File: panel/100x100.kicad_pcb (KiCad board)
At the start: 2 copper layers, 91.1 x 98.6 mm, 65 parts, among them J1 Conn_01x03_Male, J2 USB_B_Micro, SW1 SW_Push, U1 ATtiny9-TS

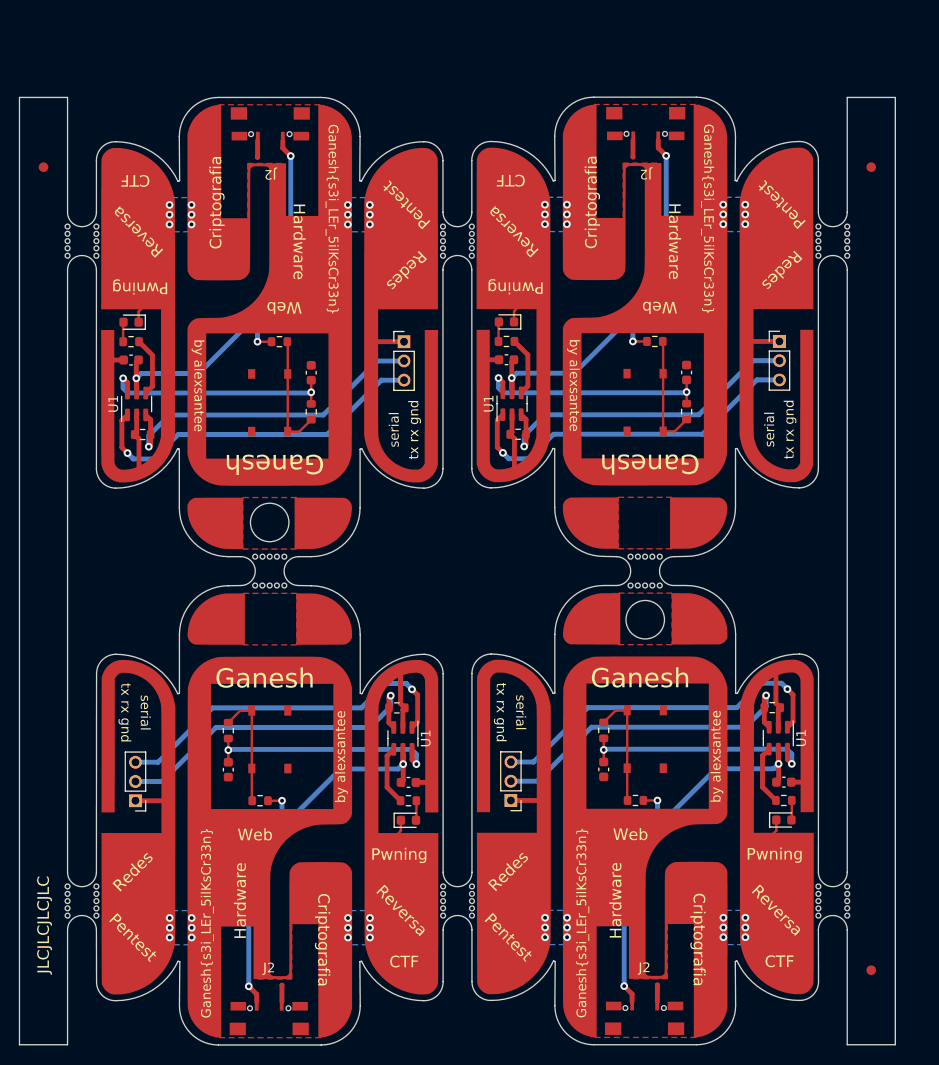
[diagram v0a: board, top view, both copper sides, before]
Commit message: panelization fixes
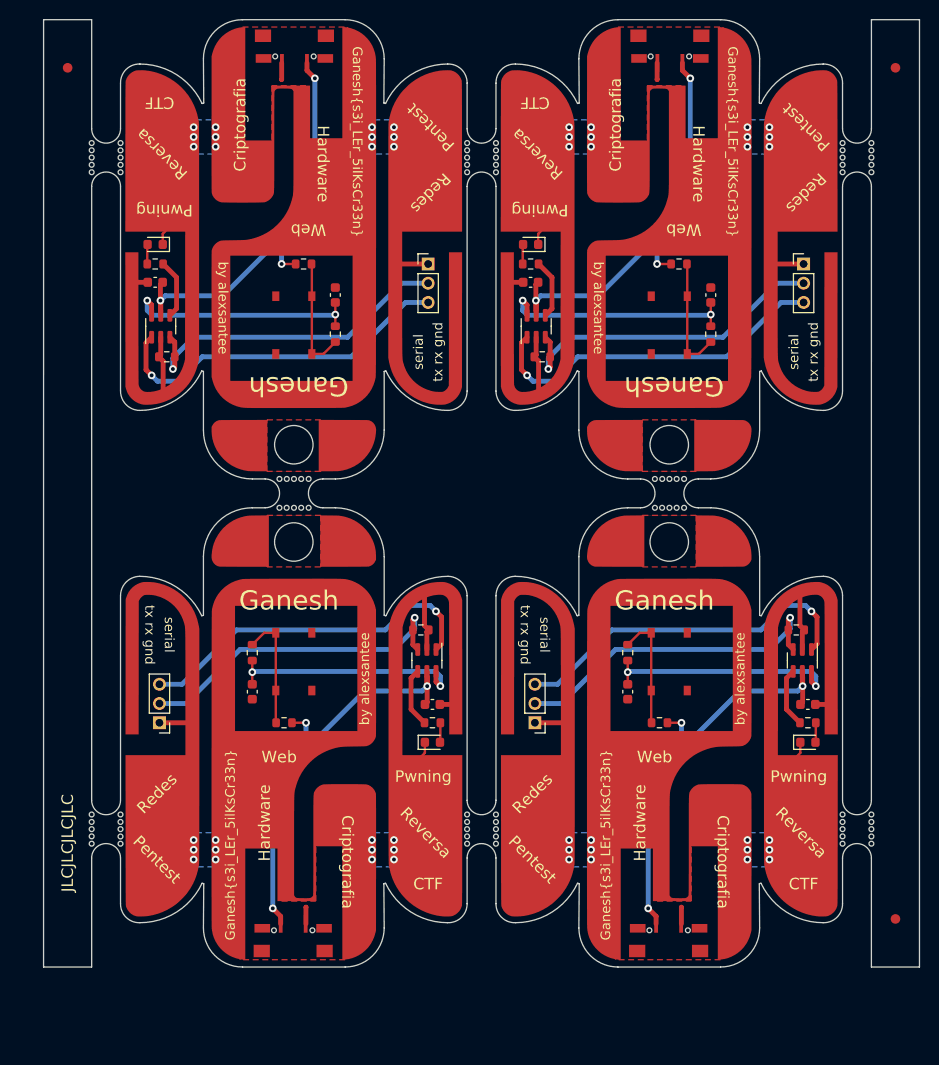
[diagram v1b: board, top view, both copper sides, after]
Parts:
- removed the C1 at (35.4, 56.8)
- removed the C1 at (74.4, 56.7)
- removed the C1 at (64.2, 100.7)
- removed the C1 at (103.3, 100.7)
- removed the C2 at (54.1, 58.1)
- removed the C2 at (93.2, 58.1)
- removed the C2 at (45.5, 99.4)
- removed the C2 at (84.5, 99.3)
- removed the D1 at (64.2, 104.6)
- removed the D1 at (74.4, 52.8)
- removed the D1 at (35.4, 52.8)
- removed the D1 at (103.3, 104.6)
- removed the Hole at (49.8, 73.7)
- removed the Hole at (88.9, 83.8)
- removed the J1 at (74.9, 102.6)
- removed the J1 at (35.9, 102.6)
- removed the J1 at (102.8, 54.8)
- removed the J1 at (63.8, 54.9)
- removed the J2 at (49.8, 127.0)
- removed the J2 at (49.9, 30.5)
- removed the J2 at (88.8, 127.0)
- removed the J2 at (88.9, 30.5)
- removed the Logo_silk at (49.8, 53.3)
- removed the Logo_silk at (88.9, 53.3)
- removed the Logo_silk at (49.8, 104.1)
- removed the Logo_silk at (88.9, 104.1)
- removed the R1 at (63.0, 92.9)
- removed the R1 at (102.1, 92.9)
- removed the R1 at (75.6, 64.5)
- removed the R1 at (36.6, 64.5)
- removed the R2 at (50.8, 54.9)
- removed the R2 at (89.9, 54.8)
- removed the R2 at (48.8, 102.6)
- removed the R2 at (87.9, 102.6)
- removed the R3 at (103.3, 102.6)
- removed the R3 at (74.4, 54.8)
- removed the R3 at (35.4, 54.9)
- removed the R3 at (64.2, 102.6)
- removed the R4 at (54.1, 62.2)
- removed the R4 at (45.5, 95.3)
- removed the R4 at (84.5, 95.3)
- removed the R4 at (93.2, 62.1)
- removed the REF** at (26.3, 36.7)
- removed the REF** at (112.4, 36.7)
- removed the REF** at (112.4, 120.2)
- removed the SW1 at (88.9, 61.2)
- removed the SW1 at (49.8, 96.2)
- removed the SW1 at (49.8, 61.2)
- removed the SW1 at (88.9, 96.2)
- removed the U1 at (36.0, 61.3)
- removed the U1 at (63.7, 96.1)
- removed the U1 at (102.7, 96.1)
- removed the U1 at (75.0, 61.3)
- removed the logo_cobre at (88.9, 53.3)
- removed the logo_cobre at (49.8, 53.3)
- removed the logo_cobre at (49.8, 104.1)
- removed the logo_cobre at (88.9, 104.1)
- removed the mouse-bite-3mm-slot at (49.8, 78.7)
- removed the mouse-bite-3mm-slot at (88.9, 78.7)
- removed the mouse-bite-3mm-slot at (69.3, 113.0)
- removed the mouse-bite-3mm-slot at (69.3, 44.4)
- removed the mouse-bite-3mm-slot at (30.3, 44.4)
- removed the mouse-bite-3mm-slot at (30.3, 113.0)
- removed the mouse-bite-3mm-slot at (108.4, 113.0)
- removed the mouse-bite-3mm-slot at (108.4, 44.4)
- added C1: 100 nF, Capacitor_SMD:C_0603_1608Metric, F.Cu at (66.7, 92.6)
- added C1: 100 nF, Capacitor_SMD:C_0603_1608Metric, F.Cu at (105.8, 92.6)
- added C1: 100 nF, Capacitor_SMD:C_0603_1608Metric, F.Cu at (76.9, 48.7)
- added C1: 100 nF, Capacitor_SMD:C_0603_1608Metric, F.Cu at (37.9, 48.7)
- added C2: 1.5 n, Capacitor_SMD:C_0603_1608Metric, F.Cu at (95.7, 50.0)
- added C2: 1.5 n, Capacitor_SMD:C_0603_1608Metric, F.Cu at (87.0, 91.3)
- added C2: 1.5 n, Capacitor_SMD:C_0603_1608Metric, F.Cu at (56.6, 50.0)
- added C2: 1.5 n, Capacitor_SMD:C_0603_1608Metric, F.Cu at (48.0, 91.3)
- added D1: LED, LED_SMD:LED_0603_1608Metric, F.Cu at (66.7, 96.5)
- added D1: LED, LED_SMD:LED_0603_1608Metric, F.Cu at (37.9, 44.8)
- added D1: LED, LED_SMD:LED_0603_1608Metric, F.Cu at (105.8, 96.5)
- added D1: LED, LED_SMD:LED_0603_1608Metric, F.Cu at (76.9, 44.8)
- added Hole: MountingHole_4mm, MountingHole:MountingHole_4mm, F.Cu at (52.3, 75.7)
- added Hole: MountingHole_4mm, MountingHole:MountingHole_4mm, F.Cu at (52.3, 65.6)
- added Hole: MountingHole_4mm, MountingHole:MountingHole_4mm, F.Cu at (91.4, 65.6)
- added Hole: MountingHole_4mm, MountingHole:MountingHole_4mm, F.Cu at (91.4, 75.7)
- added J1: Conn_01x03_Male, Connector_PinHeader_2.00mm:PinHeader_1x03_P2.00mm_Vertical, F.Cu at (66.3, 46.8)
- added J1: Conn_01x03_Male, Connector_PinHeader_2.00mm:PinHeader_1x03_P2.00mm_Vertical, F.Cu at (105.3, 46.8)
- added J1: Conn_01x03_Male, Connector_PinHeader_2.00mm:PinHeader_1x03_P2.00mm_Vertical, F.Cu at (77.4, 94.5)
- added J1: Conn_01x03_Male, Connector_PinHeader_2.00mm:PinHeader_1x03_P2.00mm_Vertical, F.Cu at (38.4, 94.5)
- added J2: USB_B_Micro, Custom_Footprints:MicroQTJ_2pads, F.Cu at (91.4, 22.4)
- added J2: USB_B_Micro, Custom_Footprints:MicroQTJ_2pads, F.Cu at (52.3, 118.9)
- added J2: USB_B_Micro, Custom_Footprints:MicroQTJ_2pads, F.Cu at (52.4, 22.4)
- added J2: USB_B_Micro, Custom_Footprints:MicroQTJ_2pads, F.Cu at (91.3, 118.9)
- added Logo_silk: LOGO, Logo_Ganesh:35x46_2, B.Cu at (52.3, 96.0)
- added Logo_silk: LOGO, Logo_Ganesh:35x46_2, B.Cu at (91.4, 45.3)
- added Logo_silk: LOGO, Logo_Ganesh:35x46_2, B.Cu at (91.4, 96.0)
- added Logo_silk: LOGO, Logo_Ganesh:35x46_2, B.Cu at (52.3, 45.3)
- added R1: 10 k, Resistor_SMD:R_0603_1608Metric, F.Cu at (104.6, 84.8)
- added R1: 10 k, Resistor_SMD:R_0603_1608Metric, F.Cu at (65.5, 84.8)
- added R1: 10 k, Resistor_SMD:R_0603_1608Metric, F.Cu at (39.1, 56.4)
- added R1: 10 k, Resistor_SMD:R_0603_1608Metric, F.Cu at (78.2, 56.4)
- added R2: 10 k, Resistor_SMD:R_0603_1608Metric, F.Cu at (90.3, 94.5)
- added R2: 10 k, Resistor_SMD:R_0603_1608Metric, F.Cu at (92.4, 46.8)
- added R2: 10 k, Resistor_SMD:R_0603_1608Metric, F.Cu at (53.3, 46.8)
- added R2: 10 k, Resistor_SMD:R_0603_1608Metric, F.Cu at (51.3, 94.5)
- added R3: 300, Resistor_SMD:R_0603_1608Metric, F.Cu at (76.9, 46.8)
- added R3: 300, Resistor_SMD:R_0603_1608Metric, F.Cu at (105.8, 94.5)
- added R3: 300, Resistor_SMD:R_0603_1608Metric, F.Cu at (66.7, 94.5)
- added R3: 300, Resistor_SMD:R_0603_1608Metric, F.Cu at (37.9, 46.8)
- added R4: 10 k, Resistor_SMD:R_0603_1608Metric, F.Cu at (48.0, 87.2)
- added R4: 10 k, Resistor_SMD:R_0603_1608Metric, F.Cu at (95.7, 54.1)
- added R4: 10 k, Resistor_SMD:R_0603_1608Metric, F.Cu at (87.0, 87.2)
- added R4: 10 k, Resistor_SMD:R_0603_1608Metric, F.Cu at (56.6, 54.1)
- added REF**: Fiducial_1mm_Mask2mm, Fiducial:Fiducial_1mm_Mask2mm, F.Cu at (114.9, 114.9)
- added REF**: Fiducial_1mm_Mask2mm, Fiducial:Fiducial_1mm_Mask2mm, F.Cu at (114.9, 26.4)
- added REF**: Fiducial_1mm_Mask2mm, Fiducial:Fiducial_1mm_Mask2mm, F.Cu at (28.8, 26.4)
- added SW1: SW_Push, Custom_Footprints:TS-1187A-B-A-B, F.Cu at (52.3, 53.1)
- added SW1: SW_Push, Custom_Footprints:TS-1187A-B-A-B, F.Cu at (91.4, 88.1)
- added SW1: SW_Push, Custom_Footprints:TS-1187A-B-A-B, F.Cu at (52.3, 88.1)
- added SW1: SW_Push, Custom_Footprints:TS-1187A-B-A-B, F.Cu at (91.4, 53.1)
- added U1: PIC10F202T-I/OT, Custom_Footprints:SOT-23-6_narrow, F.Cu at (105.2, 88.0)
- added U1: PIC10F202T-I/OT, Custom_Footprints:SOT-23-6_narrow, F.Cu at (77.5, 53.3)
- added U1: PIC10F202T-I/OT, Custom_Footprints:SOT-23-6_narrow, F.Cu at (38.5, 53.3)
- added U1: PIC10F202T-I/OT, Custom_Footprints:SOT-23-6_narrow, F.Cu at (66.2, 88.0)
- added logo_cobre: LOGO, Logo_Ganesh:35x46_2-furado, F.Cu at (52.3, 96.0)
- added logo_cobre: LOGO, Logo_Ganesh:35x46_2-furado, F.Cu at (91.4, 96.0)
- added logo_cobre: LOGO, Logo_Ganesh:35x46_2-furado, F.Cu at (52.3, 45.3)
- added logo_cobre: LOGO, Logo_Ganesh:35x46_2-furado, F.Cu at (91.4, 45.3)
- added mouse-bite-3mm-slot: VAL**, Pannelization:mouse-bite-3mm-slot, F.Cu at (32.8, 105.5)
- added mouse-bite-3mm-slot: VAL**, Pannelization:mouse-bite-3mm-slot, F.Cu at (32.8, 35.7)
- added mouse-bite-3mm-slot: VAL**, Pannelization:mouse-bite-3mm-slot, F.Cu at (52.3, 70.6)
- added mouse-bite-3mm-slot: VAL**, Pannelization:mouse-bite-3mm-slot, F.Cu at (91.4, 70.6)
- added mouse-bite-3mm-slot: VAL**, Pannelization:mouse-bite-3mm-slot, F.Cu at (110.9, 105.5)
- added mouse-bite-3mm-slot: VAL**, Pannelization:mouse-bite-3mm-slot, F.Cu at (110.9, 35.7)
- added mouse-bite-3mm-slot: VAL**, Pannelization:mouse-bite-3mm-slot, F.Cu at (71.8, 105.5)
- added mouse-bite-3mm-slot: VAL**, Pannelization:mouse-bite-3mm-slot, F.Cu at (71.8, 35.7)
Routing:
- net (no net): track 149.3 -> 0.00 mm, vias 8 -> 0
- net /button_lpout: track 0.00 -> 100.0 mm, vias 0 -> 8
- net /button_lpin: track 0.00 -> 49.3 mm
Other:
- board size 91.1 x 98.6 mm -> 91.1 x 98.5 mm
